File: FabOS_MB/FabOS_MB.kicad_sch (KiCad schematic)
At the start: 2 parts, among them U1 STM32F407VETx, U5 HF3F-L 12-1ZL1T

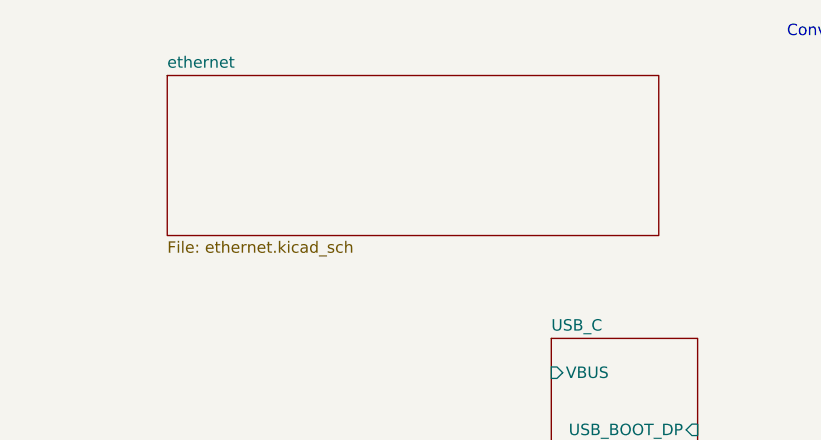
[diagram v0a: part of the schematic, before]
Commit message: ethernet pins hiérarchiques
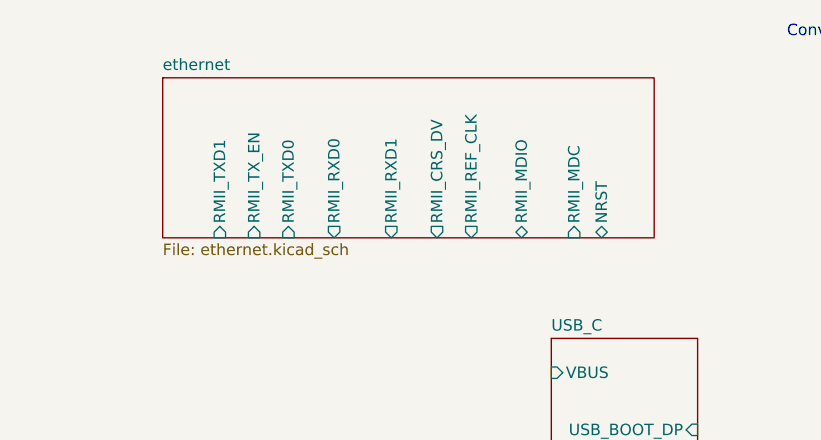
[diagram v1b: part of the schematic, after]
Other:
- sheet ethernet ports: added NRST, RMII_CRS_DV, RMII_MDC, RMII_MDIO, RMII_REF_CLK, RMII_RXD0, RMII_RXD1, RMII_TXD0, RMII_TXD1, RMII_TX_EN; removed none
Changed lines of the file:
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@@
 	)
 	(sheet
-		(at 95.25 24.13)
+		(at 94.742 24.384)
 		(size 54.61 17.78)
 		(fields_autoplaced yes)
@@
 		)
 		(property "Sheetname" "ethernet"
-			(at 95.25 23.4184 0)
+			(at 94.742 23.6724 0)
 			(effects
 				(font
@@
 		)
 		(property "Sheetfile" "ethernet.kicad_sch"
-			(at 95.25 42.4946 0)
+			(at 94.742 42.7486 0)
 			(effects
 				(font
@@
 			)
 		)
+		(pin "RMII_REF_CLK" output
+			(at 129.032 42.164 270)
+			(effects
+				(font
+					(size 1.27 1.27)
+				)
+				(justify left)
+			)
+		)
+		(pin "RMII_MDC" input
+			(at 140.462 42.164 270)
+			(effects
+				(font
+					(size 1.27 1.27)
+				)
+				(justify left)
+			)
+		)
+		(pin "RMII_CRS_DV" output
+			(at 125.222 42.164 270)
+			(effects
+				(font
+					(size 1.27 1.27)
+				)
+				(justify left)
+			)
+		)
+		(pin "RMII_RXD1" output
+			(at 120.142 42.164 270)
+			(effects
+				(font
+					(size 1.27 1.27)
+				)
+				(justify left)
+			)
+		)
+		(pin "RMII_RXD0" output
+			(at 113.792 42.164 270)
+			(effects
+				(font
+					(size 1.27 1.27)
+				)
+				(justify left)
+			)
+		)
+		(pin "RMII_TXD0" input
+			(at 108.712 42.164 270)
+			(effects
+				(font
+					(size 1.27 1.27)
+				)
+				(justify left)
+			)
+		)
+		(pin "RMII_TX_EN" input
+			(at 104.902 42.164 270)
+			(effects
+				(font
+					(size 1.27 1.27)
+				)
+				(justify left)
+			)
+		)
+		(pin "RMII_TXD1" input
+			(at 101.092 42.164 270)
+			(effects
+				(font
+					(size 1.27 1.27)
+				)
+				(justify left)
+			)
+		)
+		(pin "RMII_MDIO" bidirectional
+			(at 134.62 42.164 270)
+			(effects
+				(font
+					(size 1.27 1.27)
+				)
+				(justify left)
+			)
+		)
+		(pin "NRST" bidirectional
+			(at 143.51 42.164 270)
+			(effects
+				(font
+					(size 1.27 1.27)
+				)
+				(justify left)
+			)
+		)

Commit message: Schéma LIN
Je n'ai pas compris comment l'alim fonctionne
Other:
- sheet LIN ports: added 12V, EN, RXD, TXD; removed none
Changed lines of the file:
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@@
 			)
 		)
-		(pin "USB_BOOT_DM" input
+		(pin "USB_BOOT_DM" bidirectional
 			(at 154.178 66.04 0)
 			(effects
@@
 			)
 		)
-		(pin "USB_BOOT_DP" input
+		(pin "USB_BOOT_DP" bidirectional
 			(at 154.178 63.5 0)
 			(effects
@@
 	)
 	(sheet
-		(at 94.742 24.384)
-		(size 54.61 17.78)
+		(at 96.139 23.241)
+		(size 17.78 54.61)
 		(fields_autoplaced yes)
 		(stroke
@@
 		)
 		(property "Sheetname" "ethernet"
-			(at 94.742 23.6724 0)
+			(at 96.139 22.5294 0)
 			(effects
 				(font
@@
 		)
 		(property "Sheetfile" "ethernet.kicad_sch"
-			(at 94.742 42.7486 0)
+			(at 96.139 78.4356 0)
 			(effects
 				(font
@@
 		)
 		(pin "RMII_REF_CLK" output
-			(at 129.032 42.164 270)
+			(at 96.139 57.531 180)
 			(effects
 				(font
@@
 		)
 		(pin "RMII_MDC" input
-			(at 140.462 42.164 270)
+			(at 96.139 68.961 180)
 			(effects
 				(font
@@
 		)
 		(pin "RMII_CRS_DV" output
-			(at 125.222 42.164 270)
+			(at 96.139 53.721 180)
 			(effects
 				(font
@@
 		)
 		(pin "RMII_RXD1" output
-			(at 120.142 42.164 270)
+			(at 96.139 48.641 180)
 			(effects
 				(font
@@
 		)
 		(pin "RMII_RXD0" output
-			(at 113.792 42.164 270)
+			(at 96.139 42.291 180)
 			(effects
 				(font
@@
 		)
 		(pin "RMII_TXD0" input
-			(at 108.712 42.164 270)
+			(at 96.139 37.211 180)
 			(effects
 				(font
@@
 		)
 		(pin "RMII_TX_EN" input
-			(at 104.902 42.164 270)
+			(at 96.139 33.401 180)
 			(effects
 				(font
@@
 		)
 		(pin "RMII_TXD1" input
-			(at 101.092 42.164 270)
+			(at 96.139 29.591 180)
 			(effects
 				(font
@@
 		)
 		(pin "RMII_MDIO" bidirectional
-			(at 134.62 42.164 270)
+			(at 96.139 63.119 180)
 			(effects
 				(font
@@
 		)
 		(pin "NRST" bidirectional
-			(at 143.51 42.164 270)
+			(at 96.139 72.009 180)
 			(effects
 				(font
@@
 			)
 		)
+		(pin "12V" input
+			(at 179.07 58.42 180)
+			(effects
+				(font
+					(size 1.27 1.27)
+				)
+				(justify left)
+			)
+		)
+		(pin "EN" input
+			(at 179.07 63.5 180)
+			(effects
+				(font
+					(size 1.27 1.27)
+				)
+				(justify left)
+			)
+		)
+		(pin "TXD" input
+			(at 179.07 68.58 180)
+			(effects
+				(font
+					(size 1.27 1.27)
+				)
+				(justify left)
+			)
+		)
+		(pin "RXD" output
+			(at 209.55 63.5 0)
+			(effects
+				(font
+					(size 1.27 1.27)
+				)
+				(justify right)
+			)
+		)

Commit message: feuille switch
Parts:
- removed U5: HF3F-L 12-1ZL1T, Librairie_MB:switch 12V, symbol Librairie_MB:Switch_12V
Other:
- added sheet switch (switch.kicad_sch)
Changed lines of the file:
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@@
 		)
 	)
-	(symbol
-		(lib_id "Librairie_MB:Switch_12V")
-		(at 177.8 95.25 0)
-		(unit 1)
-		(exclude_from_sim no)
-		(in_bom yes)
-		(on_board yes)
-		(dnp no)
+	(sheet
+		(at 148.082 113.284)
+		(size 30.226 16.764)
 		(fields_autoplaced yes)
-		(property "Reference" "U5"
-			(at 177.165 85.09 0)
+		(stroke
+			(width 0.1524)
+			(type solid)
+		)
+		(fill
+			(color 0 0 0 0.0000)
+		)
+		(property "Sheetname" "switch"
+			(at 148.082 112.5724 0)
 			(effects
 				(font
 					(size 1.27 1.27)
 				)
+				(justify left bottom)
 			)
 		)
-		(property "Value" "HF3F-L 12-1ZL1T"
-			(at 177.165 87.63 0)
+		(property "Sheetfile" "switch.kicad_sch"
+			(at 148.082 130.6326 0)
 			(effects
 				(font
 					(size 1.27 1.27)
 				)
+				(justify left top)
 			)
 		)
-		(property "Footprint" "Librairie_MB:switch 12V"
-			(at 192.024 91.44 0)
-			(effects
-				(font
-					(size 1.27 1.27)
-				)
-				(hide yes)
-			)
-		)
-		(property "Datasheet" "https://www.tme.eu/Document/72a771a979a9284f42c6382232fc9181/HF3F-L.pdf"
-			(at 192.024 91.44 0)
-			(effects
-				(font
-					(size 1.27 1.27)
-				)
-				(hide yes)
-			)
-		)
-		(property "Description" "switch 12 V"
-			(at 177.165 90.17 0)
-			(effects
-				(font
-					(size 1.27 1.27)
+		(instances
+			(project "FabOS_MB"
+				(path "/09377d5d-727f-4ff4-92c8-7a0483d23f1e"
+					(page "6")
 				)
 			)
-		)
-		(property "MFR" "HF3F-L/12-1ZL1T"
-			(at 177.546 88.9 0)
-			(effects
-				(font
-					(size 1.27 1.27)
-				)
-				(hide yes)
-			)
-		)
-		(property "LCSC " "C190457"
-			(at 177.292 100.584 0)
-			(effects
-				(font
-					(size 1.27 1.27)
-				)
-				(hide yes)
-			)
-		)
-		(pin "L2"
-		)
-		(pin "1"
-		)
-		(pin "2"
-		)
-		(pin "L"
-		)
-		(pin "L1"
-		)
-		(instances
-			(project ""
-				(path "/09377d5d-727f-4ff4-92c8-7a0483d23f1e"
-					(reference "U5")
-					(unit 1)
-				)
-			)

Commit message: Maj schéma
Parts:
- added e1: Conn_01x03, Connector_Phoenix_MC_HighVoltage:PhoenixContact_MC_1,5_3-G-5.08_1x03_P5.08mm_Horizontal, symbol Connector_Generic:Conn_01x03
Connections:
- net NRST: now reaches U1.14 (NRST)
- net ETH_MDC: now reaches U1.16 (PC1)
- net ETH_REF_CLK: now reaches U1.24 (PA1)
- net ETH_MDI0: now reaches U1.25 (PA2)
- net ETH_CRS_DV: now reaches U1.32 (PA7)
- net ETH_RXD0: now reaches U1.33 (PC4)
- net ETH_RXD1: now reaches U1.34 (PC5)
- net USART3_TX: now reaches U1.47 (PB10)
- net ETH_TX_EN: now reaches U1.48 (PB11)
- net ETH_TXD0: now reaches U1.51 (PB12)
- net ETH_TXD1: now reaches U1.52 (PB13)
- net USART3_RX: now reaches U1.56 (PD9)
- net USART1_TX: now reaches U1.68 (PA9)
- net USART1_RX: now reaches U1.69 (PA10)
- new net Earth: e1.1 (Pin_1)
- new net LINE: e1.3 (Pin_3)
- new net NEUT: e1.2 (Pin_2)
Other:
- note added: "Je suis incapable de savoir si le branchement de l'USB est cohérent"
